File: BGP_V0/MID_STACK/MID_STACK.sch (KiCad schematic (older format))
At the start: 11 parts, among them P1 CONN_01X05, P2 CONN_01X09, U1 OPA170

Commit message: Gerbers
Mainly getting gerbers ready.  Issue with pots overlapping other boards in silk screens - top and bottom.
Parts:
- removed P1: CONN_01X05, Connectors_Molex:Molex_MicroLatch-53253-0570_05x2.00mm_Straight, symbol CONN_01X05
- added P1: Conn_01x05, Connectors_Molex:Molex_MicroLatch-53253-0570_05x2.00mm_Straight, symbol Conn_01x05
- U1: symbol MCP6001 -> MCP6001-RESCUE-MID_STACK
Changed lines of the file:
@@
 EESchema Schematic File Version 2
+LIBS:MID_STACK-rescue
 LIBS:power
 LIBS:device
@@
 Comment4 ""
 $EndDescr
-$Comp
-L CONN_01X05 P1
-U 1 1 5A28B76C
-P 3750 3000
-F 0 "P1" H 3750 3300 50  0000 C CNN
-F 1 "CONN_01X05" V 3850 3000 50  0000 C CNN
-F 2 "Connectors_Molex:Molex_MicroLatch-53253-0570_05x2.00mm_Straight" H 3750 3000 50  0001 C CNN
-F 3 "" H 3750 3000 50  0000 C CNN
-	1    3750 3000
-	-1   0    0    1
-$EndComp
 Text Label 3950 3200 0    60   ~ 0
 IN
@@
 F1_1
 $Comp
-L MCP6001 U1
+L MCP6001-RESCUE-MID_STACK U1
 U 1 1 5A4C5A33
 P 6300 3350
@@
 Wire Wire Line
 	7800 3600 7800 3500
+$Comp
+L Conn_01x05 P1
+U 1 1 5A573A2B
+P 3750 3000
+F 0 "P1" H 3750 3300 50  0000 C CNN
+F 1 "Conn_01x05" H 3750 2700 50  0000 C CNN
+F 2 "Connectors_Molex:Molex_MicroLatch-53253-0570_05x2.00mm_Straight" H 3750 3000 50  0001 C CNN
+F 3 "" H 3750 3000 50  0001 C CNN
+	1    3750 3000
+	-1   0    0    1
+$EndComp
 $EndSCHEMATC

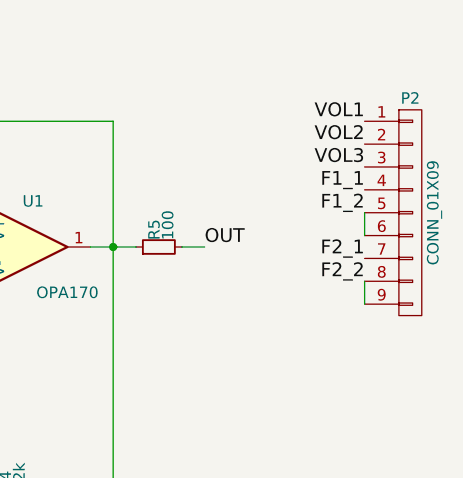
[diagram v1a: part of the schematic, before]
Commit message: Pot fixups for silkscreen overlap
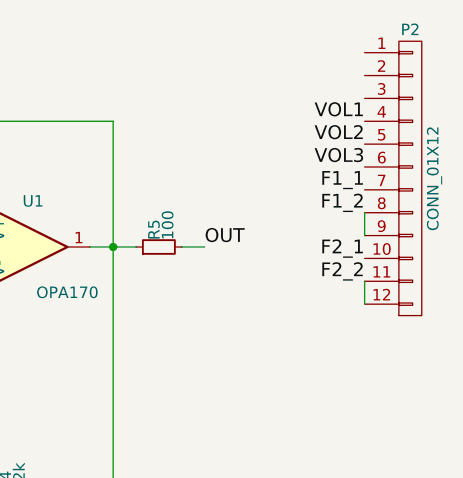
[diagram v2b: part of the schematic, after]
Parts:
- removed P2: CONN_01X09, LIBS:Potentiometer_Alpha_Tripple_Vertical_Dual_Shaft, symbol CONN_01X09
- added P2: CONN_01X12, LIBS:Potentiometer_Alps_RK097_Quad_Vertical_Dual_Shaft, symbol CONN_01X12
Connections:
- net F1_1: now also P2.10 (P10), P2.7 (P7)
- net F1_2: now also P2.8 (P8), P2.9 (P9)
- net F2_2: now also P2.11 (P11), P2.12 (P12)
- net IN: now also P2.4 (P4)
- net VOL2: now also P2.5 (P5)
- net VOL3: now also P2.6 (P6)
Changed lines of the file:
@@
 V-
 $Comp
-L Earth #PWR01
+L Earth #PWR1
 U 1 1 5A4C5085
 P 3950 3000
-F 0 "#PWR01" H 3950 2750 50  0001 C CNN
+F 0 "#PWR1" H 3950 2750 50  0001 C CNN
 F 1 "Earth" H 3950 2850 50  0001 C CNN
 F 2 "" H 3950 3000 50  0000 C CNN
@@
 Connection ~ 5750 4100
 $Comp
-L Earth #PWR02
+L Earth #PWR2
 U 1 1 5A4C5CFC
 P 5750 4150
-F 0 "#PWR02" H 5750 3900 50  0001 C CNN
+F 0 "#PWR2" H 5750 3900 50  0001 C CNN
 F 1 "Earth" H 5750 4000 50  0001 C CNN
 F 2 "" H 5750 4150 50  0000 C CNN
@@
 Text Label 7100 3350 0    60   ~ 0
 OUT
-$Comp
-L CONN_01X09 P2
-U 1 1 5A4C61D7
-P 8000 3200
-F 0 "P2" H 8000 3700 50  0000 C CNN
-F 1 "CONN_01X09" V 8100 3200 50  0000 C CNN
-F 2 "LIBS:Potentiometer_Alpha_Tripple_Vertical_Dual_Shaft" H 8000 3200 50  0001 C CNN
-F 3 "" H 8000 3200 50  0000 C CNN
-	1    8000 3200
-	1    0    0    -1
-$EndComp
 Text Label 7800 2800 2    60   ~ 0
 VOL1
@@
 	-1   0    0    1
 $EndComp
+$Comp
+L CONN_01X12 P2
+U 1 1 5A5803F1
+P 8000 3050
+F 0 "P2" H 8000 3700 50  0000 C CNN
+F 1 "CONN_01X12" V 8100 3050 50  0000 C CNN
+F 2 "LIBS:Potentiometer_Alps_RK097_Quad_Vertical_Dual_Shaft" H 8000 3050 50  0001 C CNN
+F 3 "" H 8000 3050 50  0000 C CNN
+	1    8000 3050
+	1    0    0    -1
+$EndComp
 $EndSCHEMATC

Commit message: V_0 Updates for caps, gerbers updated
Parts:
- C1: value 10u -> 22u
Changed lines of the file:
@@
 P 4350 3000
 F 0 "C1" H 4360 3070 50  0000 L CNN
-F 1 "10u" H 4360 2920 50  0000 L CNN
+F 1 "22u" H 4360 2920 50  0000 L CNN
 F 2 "Capacitors_SMD:C_1206_HandSoldering" H 4350 3000 50  0001 C CNN
 F 3 "" H 4350 3000 50  0000 C CNN
@@
 V-
 $Comp
-L Earth #PWR1
+L Earth #PWR01
 U 1 1 5A4C5085
 P 3950 3000
-F 0 "#PWR1" H 3950 2750 50  0001 C CNN
+F 0 "#PWR01" H 3950 2750 50  0001 C CNN
 F 1 "Earth" H 3950 2850 50  0001 C CNN
 F 2 "" H 3950 3000 50  0000 C CNN
@@
 Connection ~ 5750 4100
 $Comp
-L Earth #PWR2
+L Earth #PWR02
 U 1 1 5A4C5CFC
 P 5750 4150
-F 0 "#PWR2" H 5750 3900 50  0001 C CNN
+F 0 "#PWR02" H 5750 3900 50  0001 C CNN
 F 1 "Earth" H 5750 4000 50  0001 C CNN
 F 2 "" H 5750 4150 50  0000 C CNN

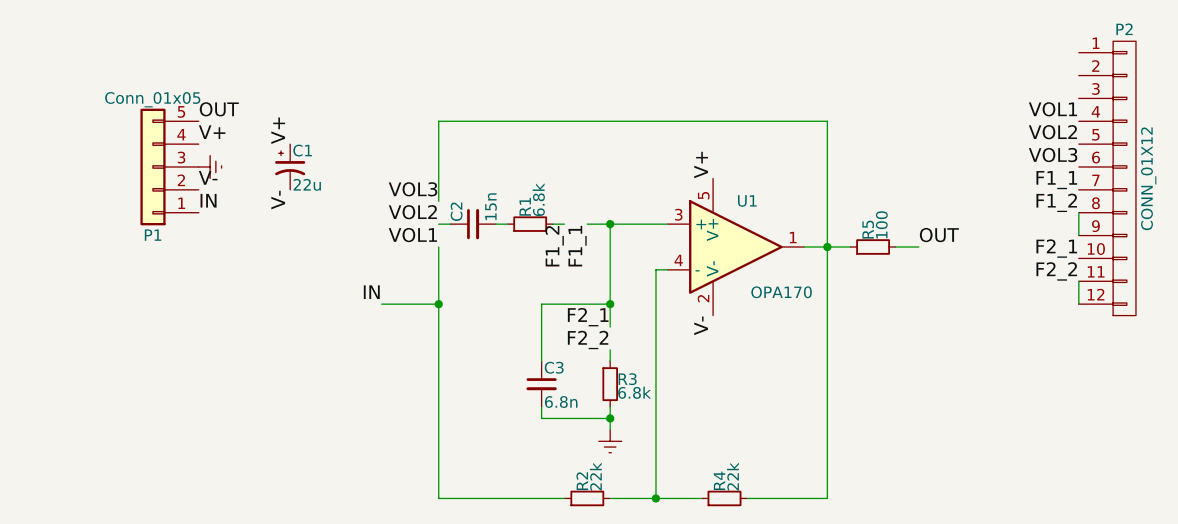
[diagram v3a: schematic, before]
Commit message: Changed Mid sweep
200 - 2k Hz
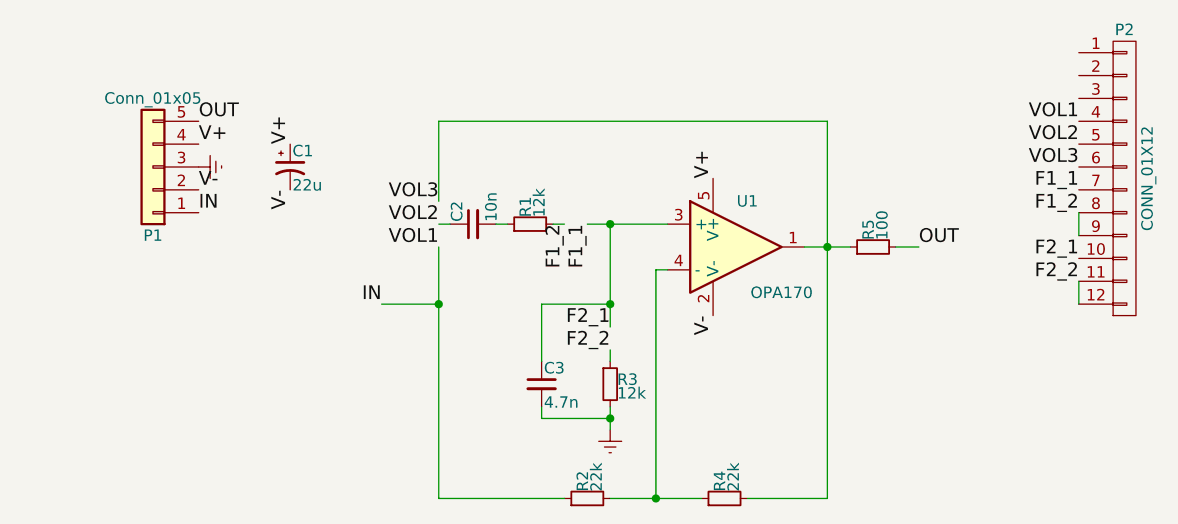
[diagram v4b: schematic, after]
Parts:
- C2: value 15n -> 10n; footprint Capacitors_SMD:C_1206_HandSoldering -> Capacitors_SMD:C_0805_HandSoldering
- C3: value 6.8n -> 4.7n
- R1, R3: value 6.8k -> 12k
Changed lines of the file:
@@
 P 5150 3250
 F 0 "C2" H 5160 3320 50  0000 L CNN
-F 1 "15n" H 5160 3170 50  0000 L CNN
-F 2 "Capacitors_SMD:C_1206_HandSoldering" H 5150 3250 50  0001 C CNN
+F 1 "10n" H 5160 3170 50  0000 L CNN
+F 2 "Capacitors_SMD:C_0805_HandSoldering" H 5150 3250 50  0001 C CNN
 F 3 "" H 5150 3250 50  0000 C CNN
 	1    5150 3250
@@
 P 5400 3250
 F 0 "R1" H 5430 3270 50  0000 L CNN
-F 1 "6.8k" H 5430 3210 50  0000 L CNN
+F 1 "12k" H 5430 3210 50  0000 L CNN
 F 2 "Resistors_SMD:R_0603_HandSoldering" H 5400 3250 50  0001 C CNN
 F 3 "" H 5400 3250 50  0000 C CNN
@@
 P 5750 3950
 F 0 "R3" H 5780 3970 50  0000 L CNN
-F 1 "6.8k" H 5780 3910 50  0000 L CNN
+F 1 "12k" H 5780 3910 50  0000 L CNN
 F 2 "Resistors_SMD:R_0603_HandSoldering" H 5750 3950 50  0001 C CNN
 F 3 "" H 5750 3950 50  0000 C CNN
@@
 P 5450 3950
 F 0 "C3" H 5460 4020 50  0000 L CNN
-F 1 "6.8n" H 5460 3870 50  0000 L CNN
+F 1 "4.7n" H 5460 3870 50  0000 L CNN
 F 2 "Capacitors_SMD:C_0805_HandSoldering" H 5450 3950 50  0001 C CNN
 F 3 "" H 5450 3950 50  0000 C CNN
